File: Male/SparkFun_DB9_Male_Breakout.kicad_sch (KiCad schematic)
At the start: 12 parts, among them J2 Conn_01x09, J3 DE9-Male

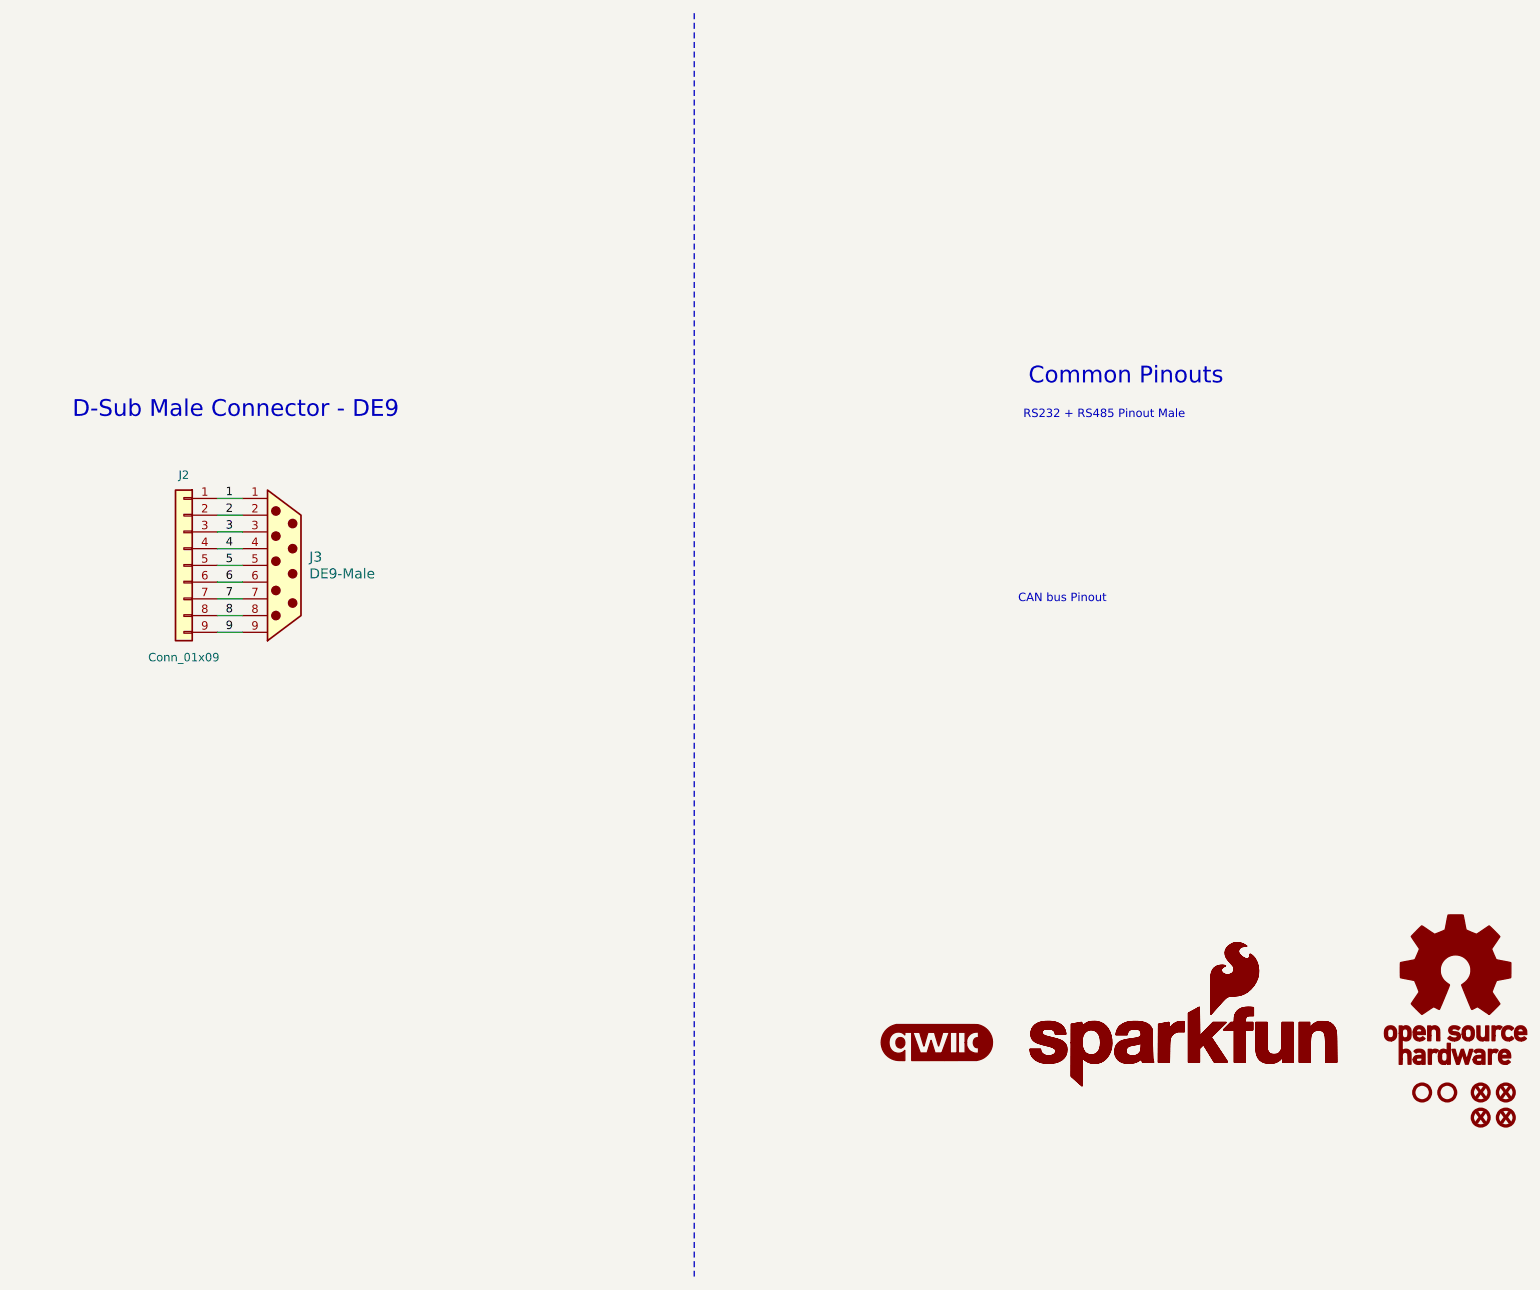
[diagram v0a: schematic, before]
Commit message: Adds some underbars to numbers, adds silk to bottom side on male DB9
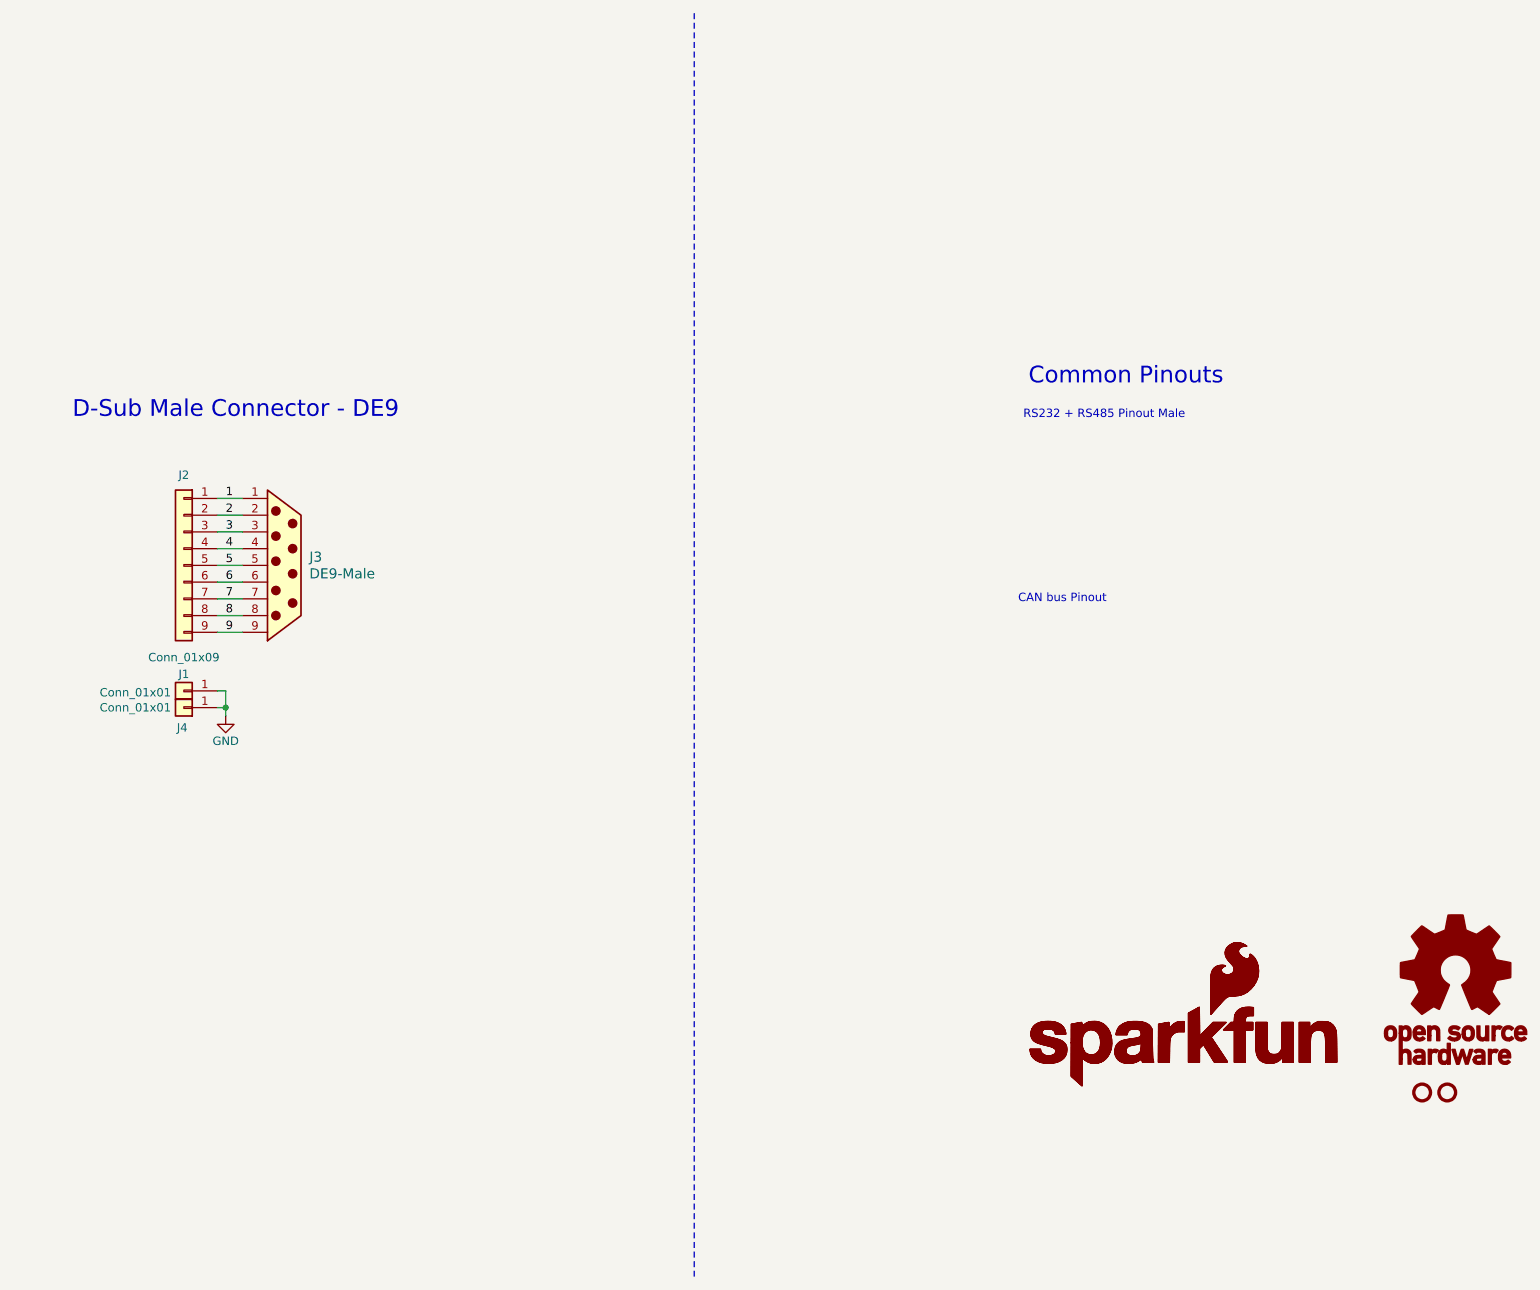
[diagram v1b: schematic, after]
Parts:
- removed FID1, FID2, FID3, FID4: Fiducial_0.5mm, SparkFun-Aesthetic:Fiducial_0.5mm_Mask1mm, symbol SparkFun-Aesthetic:Fiducial_0.5mm
- removed G4: qwiic_Logo, symbol SparkFun-Aesthetic:qwiic_Logo
- added J1, J4: Conn_01x01, SparkFun-Connector:1x01, symbol SparkFun-Connector:Conn_01x01
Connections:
- new net GND: J1.1 (Pin_1), J4.1 (Pin_1)
